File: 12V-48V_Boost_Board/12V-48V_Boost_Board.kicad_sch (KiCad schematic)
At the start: 12 parts, among them J1 12V Input, J2 Input Current Sensing, J3 Output Current Sensing, J4 48V Output, J5 Output Measuring

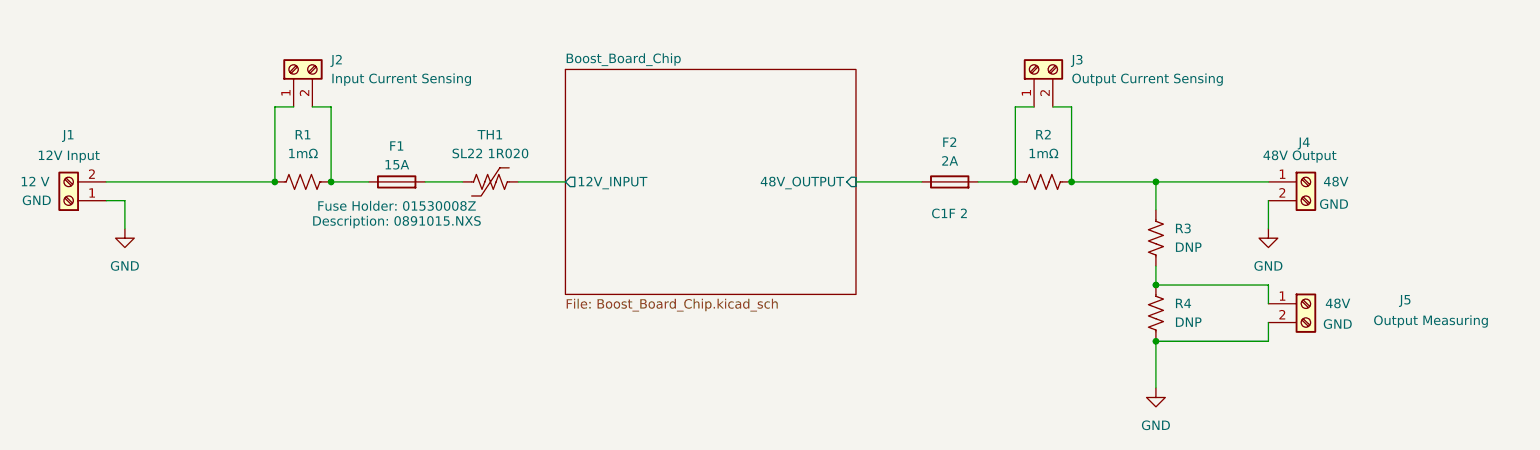
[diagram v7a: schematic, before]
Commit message: Updated as review, let me know if I should just redo the layout completely cause its still a bit scuffed imo
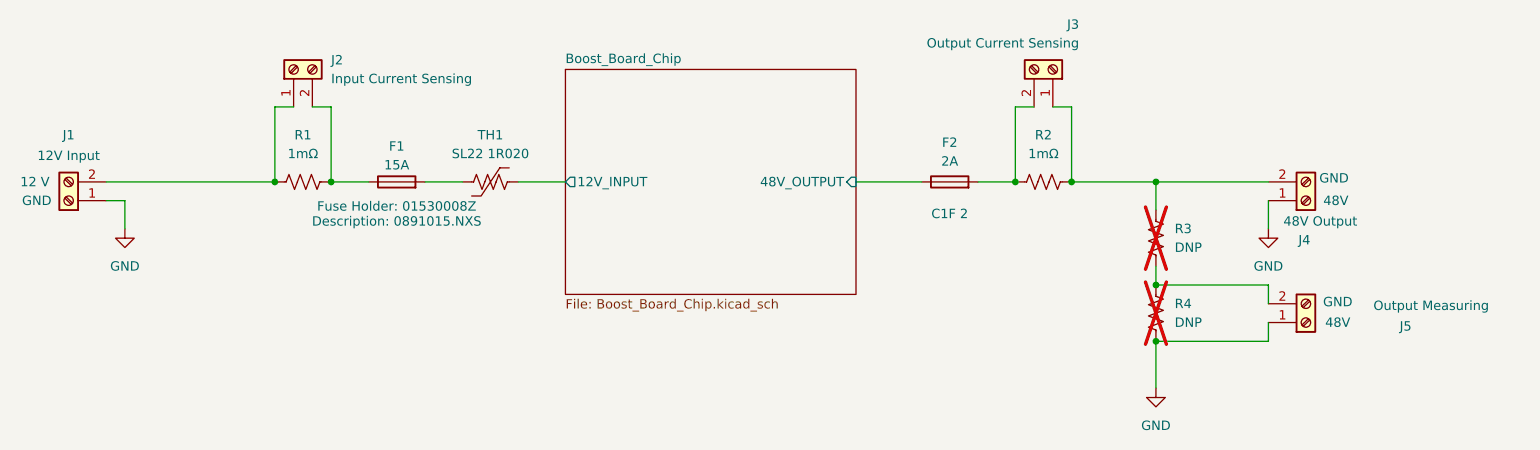
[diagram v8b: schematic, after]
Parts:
- R3, R4: now not fitted
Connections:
- net GND: now also J4.1 (Pin_1), J5.1 (Pin_1); no longer J4.2 (Pin_2), J5.2 (Pin_2)
- net at R3.1, R4.2: now also J5.2 (Pin_2); no longer J5.1 (Pin_1)
- net at R2.2, R3.2: now also J3.1 (Pin_1), J4.2 (Pin_2); no longer J3.2 (Pin_2), J4.1 (Pin_1)
- net at F2.2, R2.1: now also J3.2 (Pin_2); no longer J3.1 (Pin_1)
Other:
- moved on the sheet: J3
